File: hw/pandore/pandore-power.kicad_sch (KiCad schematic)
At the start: 0 parts

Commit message: added all remaining connectors (only missing M.2 now)
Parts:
- added J6: VIN, reekilib_con:samesky_PJ-063BH, symbol reekilib_con:barrel_shield
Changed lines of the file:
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@@
 		(company "${corp}")
 	)
+	(symbol
+		(lib_id "reekilib_con:barrel_shield")
+		(at 31.75 33.02 0)
+		(unit 1)
+		(exclude_from_sim no)
+		(in_bom yes)
+		(on_board yes)
+		(dnp no)
+		(fields_autoplaced yes)
+		(property "Reference" "J6"
+			(at 31.75 24.13 0)
+			(do_not_autoplace yes)
+			(effects
+				(font
+					(size 1 1)
+				)
+			)
+		)
+		(property "Value" "VIN"
+			(at 26.035 31.75 90)
+			(do_not_autoplace yes)
+			(effects
+				(font
+					(size 1 1)
+				)
+			)
+		)
+		(property "Footprint" "reekilib_con:samesky_PJ-063BH"
+			(at 31.75 49.53 0)
+			(do_not_autoplace yes)
+			(effects
+				(font
+					(size 1 1)
+				)
+				(hide yes)
+			)
+		)
+		(property "Datasheet" "https://www.sameskydevices.com/product/resource/pj-063bh.pdf"
+			(at 31.75 48.26 0)
+			(do_not_autoplace yes)
+			(effects
+				(font
+					(size 1 1)
+				)
+				(hide yes)
+			)
+		)
+		(property "Description" "Barrel connector"
+			(at 31.75 46.99 0)
+			(do_not_autoplace yes)
+			(effects
+				(font
+					(size 1 1)
+				)
+				(hide yes)
+			)
+		)
+		(property "Vmax" "24V"
+			(at 27.305 45.72 0)
+			(do_not_autoplace yes)
+			(effects
+				(font
+					(size 1 1)
+				)
+				(hide yes)
+			)
+		)
+		(property "Imax" "8A"
+			(at 31.75 45.72 0)
+			(do_not_autoplace yes)
+			(effects
+				(font
+					(size 1 1)
+				)
+				(hide yes)
+			)
+		)
+		(property "MPN" "PJ-063BH"
+			(at 31.75 41.91 0)
+			(do_not_autoplace yes)
+			(effects
+				(font
+					(size 1 1)
+				)
+				(hide yes)
+			)
+		)
+		(property "MFG" "Same sky"
+			(at 44.45 41.91 0)
+			(do_not_autoplace yes)
+			(effects
+				(font
+					(size 1 1)
+				)
+				(justify left)
+				(hide yes)
+			)
+		)
+		(property "Link" "https://www.sameskydevices.com/product/interconnect/connectors/dc-power-connectors/jacks/pj-063bh"
+			(at 61.595 41.91 0)
+			(do_not_autoplace yes)
+			(effects
+				(font
+					(size 1 1)
+				)
+				(justify left)
+				(hide yes)
+			)
+		)
+		(pin "3"
+		)
+		(pin "1"
+		)
+		(pin "2"
+		)
+		(pin "S"
+		)
+		(instances
+			(project ""
+				(path "/e55f2700-f75a-4062-8a27-fe258faa8966/13357c90-191e-461b-8733-0658b5b931ff"
+					(reference "J6")
+					(unit 1)
+				)
+			)
+		)
+	)
 )

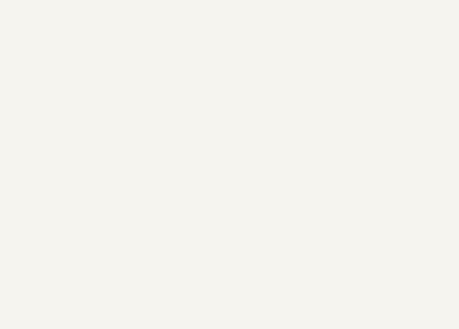
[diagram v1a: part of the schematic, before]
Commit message: Added lots to sch and pcb: eth passive, audio codec, midi, teensy Corrected and added support for M.2
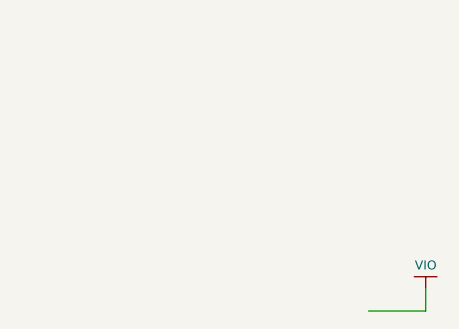
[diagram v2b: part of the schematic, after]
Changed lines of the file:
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@@
 		(company "${corp}")
+	)
+	(wire
+		(pts
+			(xy 259.08 102.87) (xy 259.08 105.41)
+		)
+		(stroke
+			(width 0)
+			(type default)
+		)
+	)
+	(wire
+		(pts
+			(xy 252.73 105.41) (xy 259.08 105.41)
+		)
+		(stroke
+			(width 0)
+			(type default)
+		)
+	)
+	(netclass_flag ""
+		(length 1.27)
+		(shape diamond)
+		(at 254 105.41 0)
+		(fields_autoplaced yes)
+		(effects
+			(font
+				(size 1.016 1.016)
+			)
+			(justify left bottom)
+		)
+		(property "Netclass" "PWR"
+			(at 255.0973 104.14 0)
+			(effects
+				(font
+					(size 1.27 1.27)
+				)
+				(justify left)
+			)
+		)
+		(property "Component Class" ""
+			(at 80.01 68.58 0)
+			(effects
+				(font
+					(size 1.27 1.27)
+					(italic yes)
+				)
+			)
+		)
+	)
+	(symbol
+		(lib_id "reekilib_pwr:VDD")
+		(at 259.08 101.6 0)
+		(unit 1)
+		(exclude_from_sim no)
+		(in_bom no)
+		(on_board no)
+		(dnp no)
+		(property "Reference" "#PWR0102"
+			(at 259.08 98.425 0)
+			(do_not_autoplace yes)
+			(effects
+				(font
+					(size 1 1)
+				)
+				(hide yes)
+			)
+		)
+		(property "Value" "VIO"
+			(at 259.08 100.33 0)
+			(effects
+				(font
+					(size 1 1)
+				)
+			)
+		)
+		(property "Footprint" ""
+			(at 259.08 101.6 0)
+			(effects
+				(font
+					(size 1.524 1.524)
+				)
+			)
+		)
+		(property "Datasheet" ""
+			(at 259.08 101.6 0)
+			(effects
+				(font
+					(size 1.524 1.524)
+				)
+			)
+		)
+		(property "Description" ""
+			(at 259.08 101.6 0)
+			(effects
+				(font
+					(size 1.27 1.27)
+				)
+				(hide yes)
+			)
+		)
+		(pin "1"
+		)
+		(instances
+			(project "pandore"
+				(path "/e55f2700-f75a-4062-8a27-fe258faa8966/13357c90-191e-461b-8733-0658b5b931ff"
+					(reference "#PWR0102")
+					(unit 1)
+				)
+			)
+		)
 	)
 	(symbol

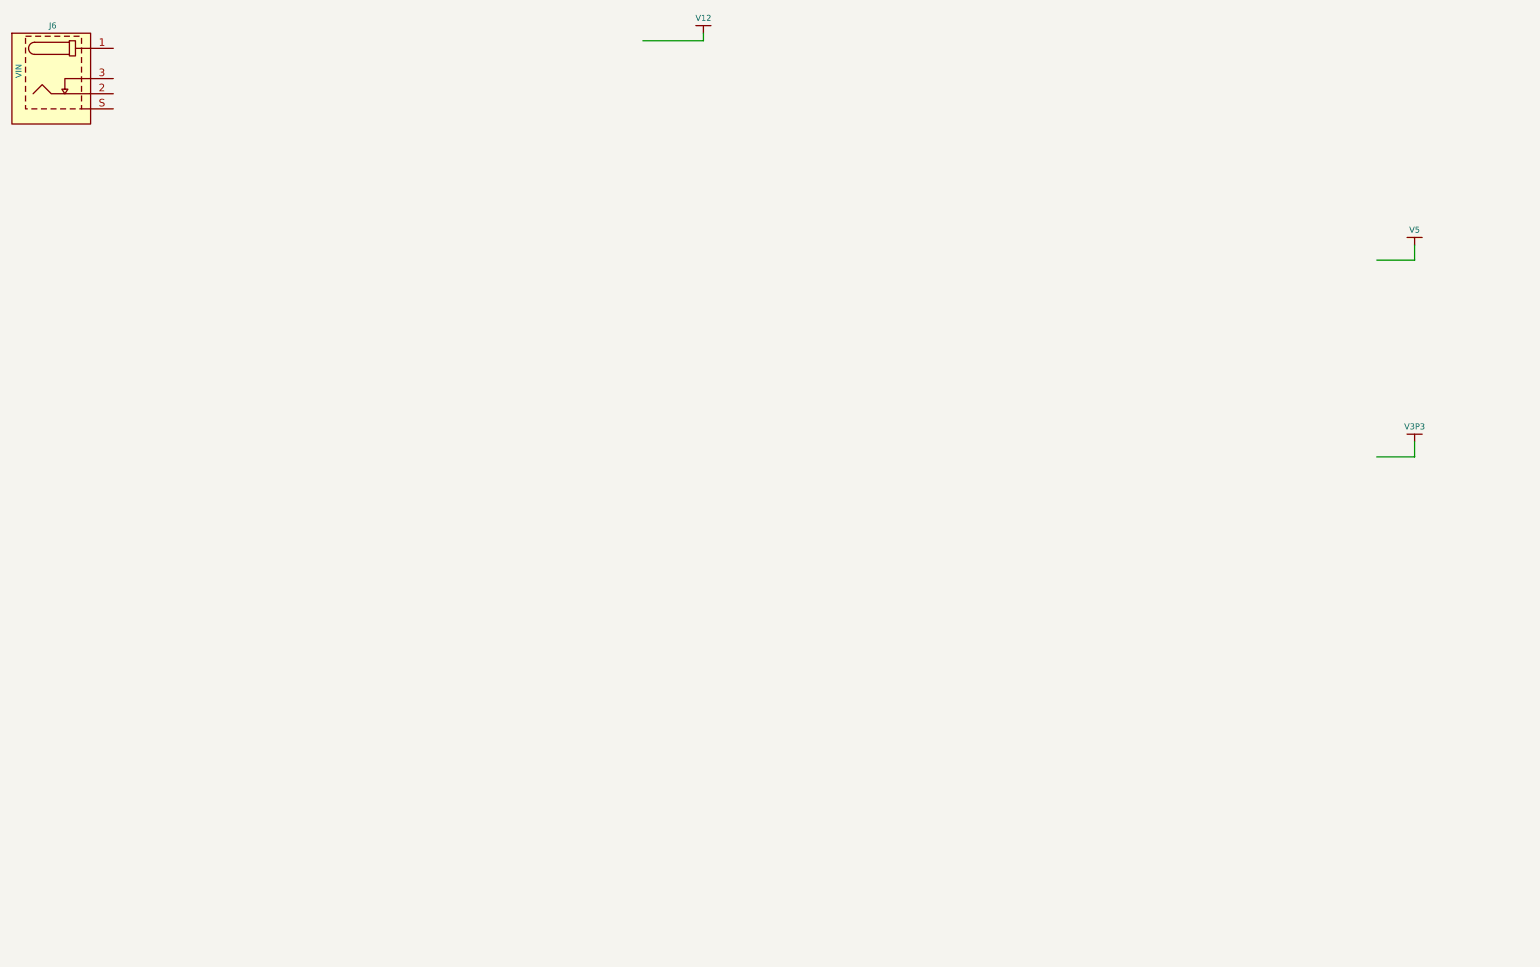
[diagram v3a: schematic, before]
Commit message: added power stuff revised M.2 for higher model and added m.2 mounts added power tap terminals
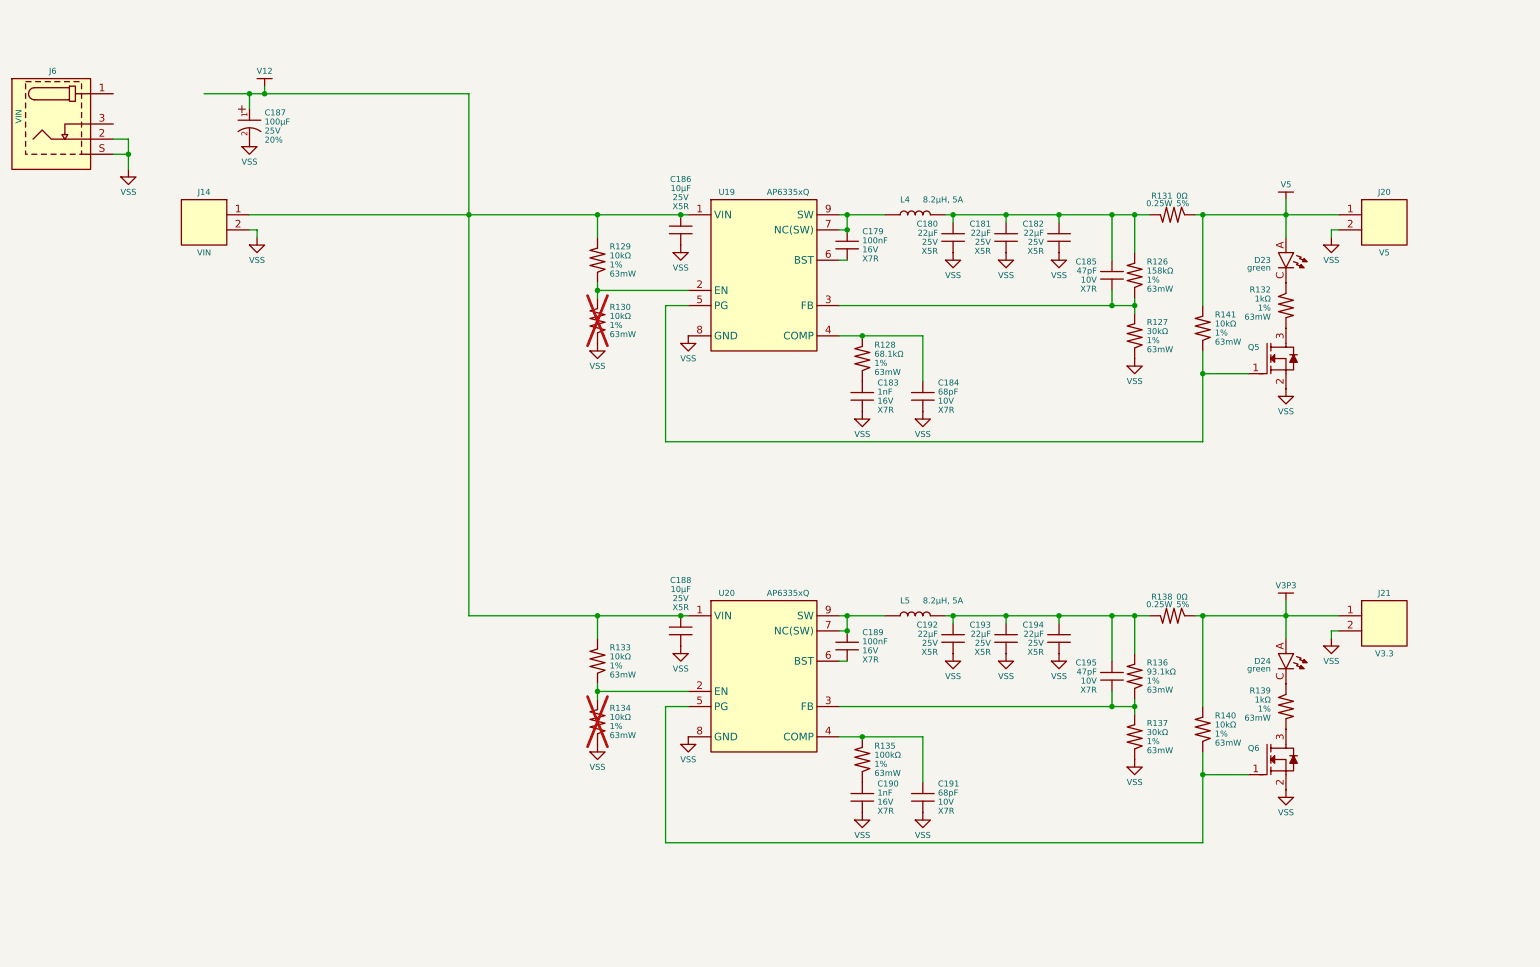
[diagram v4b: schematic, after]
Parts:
- added C179, C183, C184, C185, C189, C190, C191, C195: ${Capacitance}, ${Voltage}, ${Dielectric}, reekilib_cap:CAPC1005, symbol reekilib_cap:cap
- added C180, C181, C182, C192, C193, C194: ${Capacitance}, ${Voltage}, ${Dielectric}, reekilib_cap:CAPC3216, symbol reekilib_cap:cap
- added C186, C188: ${Capacitance}, ${Voltage}, ${Dielectric}, reekilib_cap:CAPC2012, symbol reekilib_cap:cap
- added C187: ${Capacitance}, ${Voltage}, ${Tolerance}, reekilib_cap:CAPAE630Xxxx, symbol reekilib_cap:cap_pol
- added D23, D24: ${color}, reekilib_led:LEDM1608X80, symbol reekilib_led:led
- added J14: VIN, reekilib_con:Wurth_691137710002, symbol reekilib_con:hdr-1x2
- added J20: V5, reekilib_con:Wurth_691137710002, symbol reekilib_con:hdr-1x2
- added J21: V3.3, reekilib_con:Wurth_691137710002, symbol reekilib_con:hdr-1x2
- added L4, L5: 8.2µH, 5A, reekilib_ind:Eaton_HPAL1V0630, symbol reekilib_ind:ind
- added Q5, Q6: MOSFET_EN-N, reekilib_sot:SOT95P280X100-3, symbol reekilib_mfe:MOSFET_EN-N
- added R126, R127, R128, R129, R130, R132, R133, R134, R135, R136, R137, R139, R140, R141: ${Resistance}, ${Tolerance}, ${Power}, reekilib_res:RESC1005, symbol reekilib_res:res
- added R131, R138: ${Resistance}, ${Tolerance}, ${Type}, reekilib_res:RESC2012, symbol reekilib_res:res
- added U19, U20: AP6335xQ, reekilib_dfn:DFN300X200X90-9, symbol reekilib_swr:AP6335xQ
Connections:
- net V12: now also C186.2, C187.1 (+), C188.2, J14.1, R129.1, R133.1, U19.1 (VIN), U20.1 (VIN)
- net V3P3: now also D24.A, J21.1, R138.2, R140.1
- net V5: now also D23.A, J20.1, R131.2, R141.1
- net VSS: now reaches J6.2 (RING)
- net VSS: now also J6.S (SHD), C180.1, C181.1, C182.1, C183.1, C184.1, C186.1, C187.2 (-), C188.1, C190.1, C191.1, C192.1, C193.1, C194.1, J14.2, J20.2, J21.2, Q5.2 (S), Q6.2 (S), R127.2, R130.2, R134.2, R137.2, U19.8 (GND), U20.8 (GND)
- new net: C185.1, R126.2, R127.1, U19.3 (FB)
- new net: C180.2, C181.2, C182.2, C185.2, L4.2, R126.1, R131.1
- new net: C183.2, R128.2
- new net: C192.2, C193.2, C194.2, C195.2, L5.2, R136.1, R138.1
- new net: C191.2, R135.1, U20.4 (COMP)
- new net: C184.2, R128.1, U19.4 (COMP)
- new net: R129.2, R130.1, U19.2 (EN)
- new net: C179.2, L4.1, U19.7 (NC(SW)), U19.9 (SW)
- new net: C179.1, U19.6 (BST)
- new net: C190.2, R135.2
- new net: R133.2, R134.1, U20.2 (EN)
- new net: C195.1, R136.2, R137.1, U20.3 (FB)
- new net: Q6.1 (G), R140.2, U20.5 (PG)
- new net: C189.1, U20.6 (BST)
- new net: C189.2, L5.1, U20.7 (NC(SW)), U20.9 (SW)
- new net: D24.C, R139.2
- new net: Q6.3 (D), R139.1
- new net: Q5.1 (G), R141.2, U19.5 (PG)
- new net: D23.C, R132.2
- new net: Q5.3 (D), R132.1
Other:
- moved on the sheet: J6

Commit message: most of board control signals added, routed and defined
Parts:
- added C259: ${Capacitance}, ${Voltage}, ${Dielectric}, reekilib_cap:CAPC2012, symbol reekilib_cap:cap
- added C260, C261: ${Capacitance}, ${Voltage}, ${Dielectric}, reekilib_cap:CAPC1005, symbol reekilib_cap:cap
- added D33: ${color}, reekilib_led:LEDM1608X80, symbol reekilib_led:led
- added J32: VSTBY, reekilib_con:HDR254P1X02-TH, symbol reekilib_con:hdr-1x2
- added R223, R224, R225, R226, R228: ${Resistance}, ${Tolerance}, ${Power}, reekilib_res:RESC1005, symbol reekilib_res:res
- added R227: ${Resistance}, ${Tolerance}, ${Type}, reekilib_res:RESC2012, symbol reekilib_res:res
- added U27: LDL212DR, reekilib_soic:SOIC127P600X150-8, symbol reekilib_ldo:LDL212
- D23, D24: Link https://ams-osram.com/products/leds/color-leds/osram-smartled-0603-kt-eelp41-12 -> https://ams-osram.com/products/leds/color-leds/osram-smartled-0603-ko-eelp41-22; Vf 2.5V -> 2.0V; Vr 1.2V -> 10V; color green -> orange; lum 224mcd@5mA -> 392mcd@5mA; λdom 527nm -> 610nm
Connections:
- net V12: now also C259.2, R223.1, U27.4 (IN)
- net VSS: now also C259.1, C260.1, C261.1, J32.1, R224.2, R226.2, R228.1, U27.2 (GND), U27.3 (GND), U27.6 (GND), U27.7 (GND)
- new net: D33.C, R228.2
- new net: C260.2, C261.2, R225.1, R227.1, U27.1 (OUT)
- new net: R225.2, R226.1, U27.8 (FB)
- new net: R223.2, R224.1, U27.5 (EN)
- new net VSTBY: D33.A, J32.2, R227.2
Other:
- note added: "TODO: actual vout calc"
- note added: "TODO: enable setting"
- moved on the sheet: C188, C189, C190, C191, C192, C193, C194, C195, J21, L5, Q6, R133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

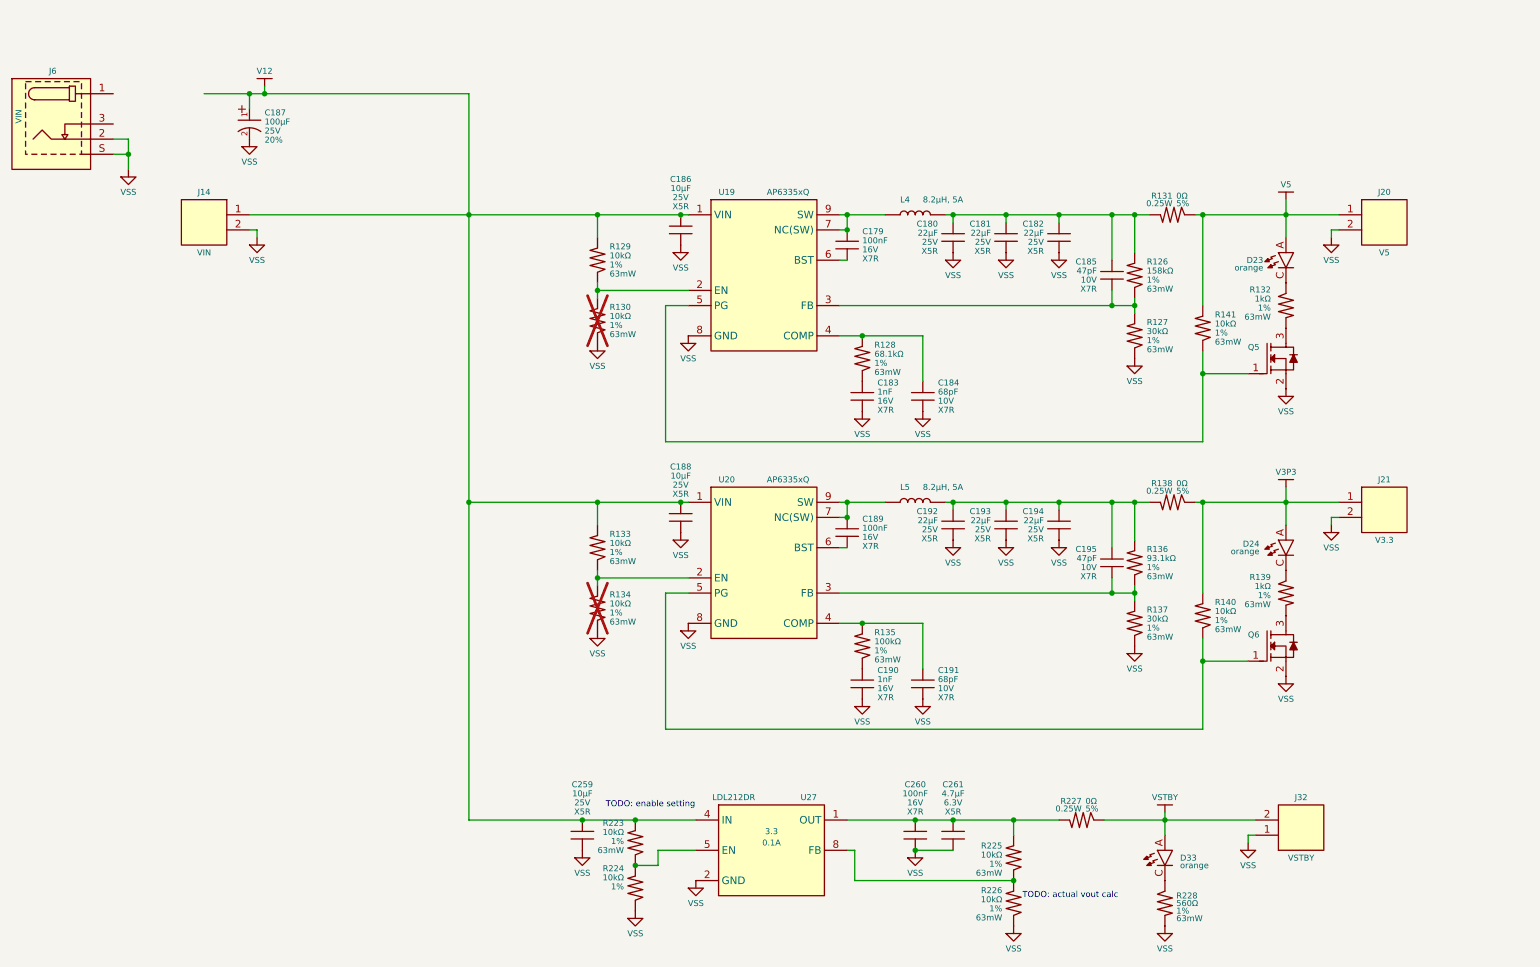
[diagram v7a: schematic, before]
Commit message: more routing/placement done added 5v load switch 1A each added second fan circuit redone all diffpair routing following new stackup calc added all (?) missing connectors to unused pins
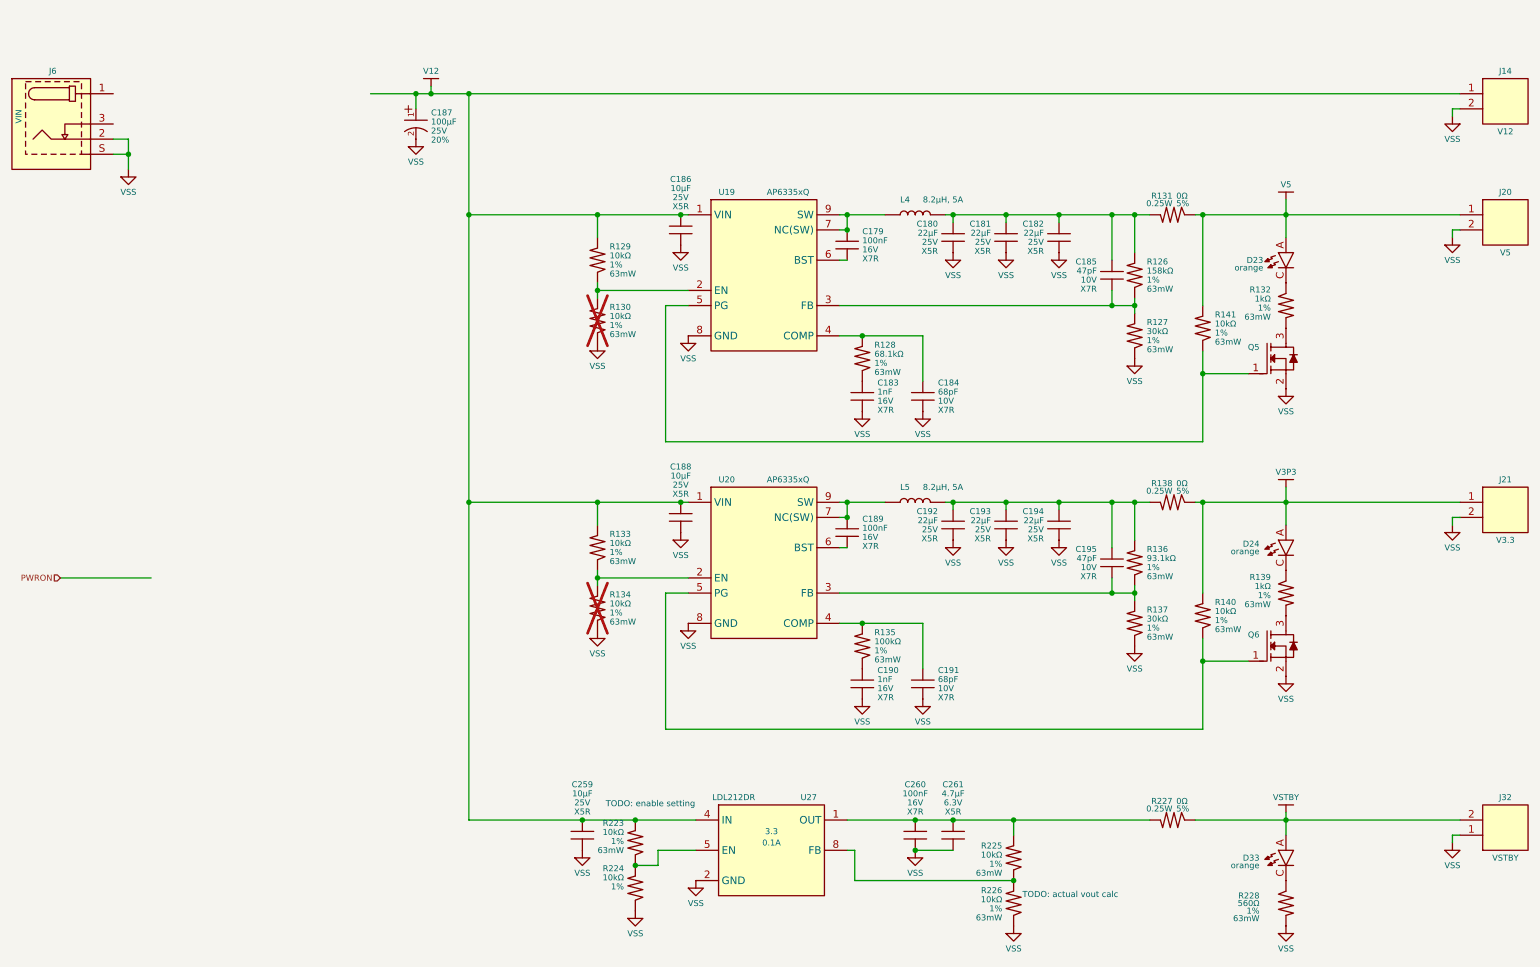
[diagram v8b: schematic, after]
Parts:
- J14: value VIN -> V12
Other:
- moved on the sheet: C187, D33, J14, J20, J21, J32, R227, R228
